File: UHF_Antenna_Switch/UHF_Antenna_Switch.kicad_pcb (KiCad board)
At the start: 2 copper layers, 157.2 x 60 mm, 44 parts, among them J1 Conn_N_Type_Female, J2 Conn_SO-239, J3 Conn_SMA_Female, J4 Screw_Terminal_01x04, J5 Conn_02x03_Odd_Even, K1 HF3-51, K2 HF3-51, Q2 2N7002, Q3 2N7002, SW1 SW_SP3T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

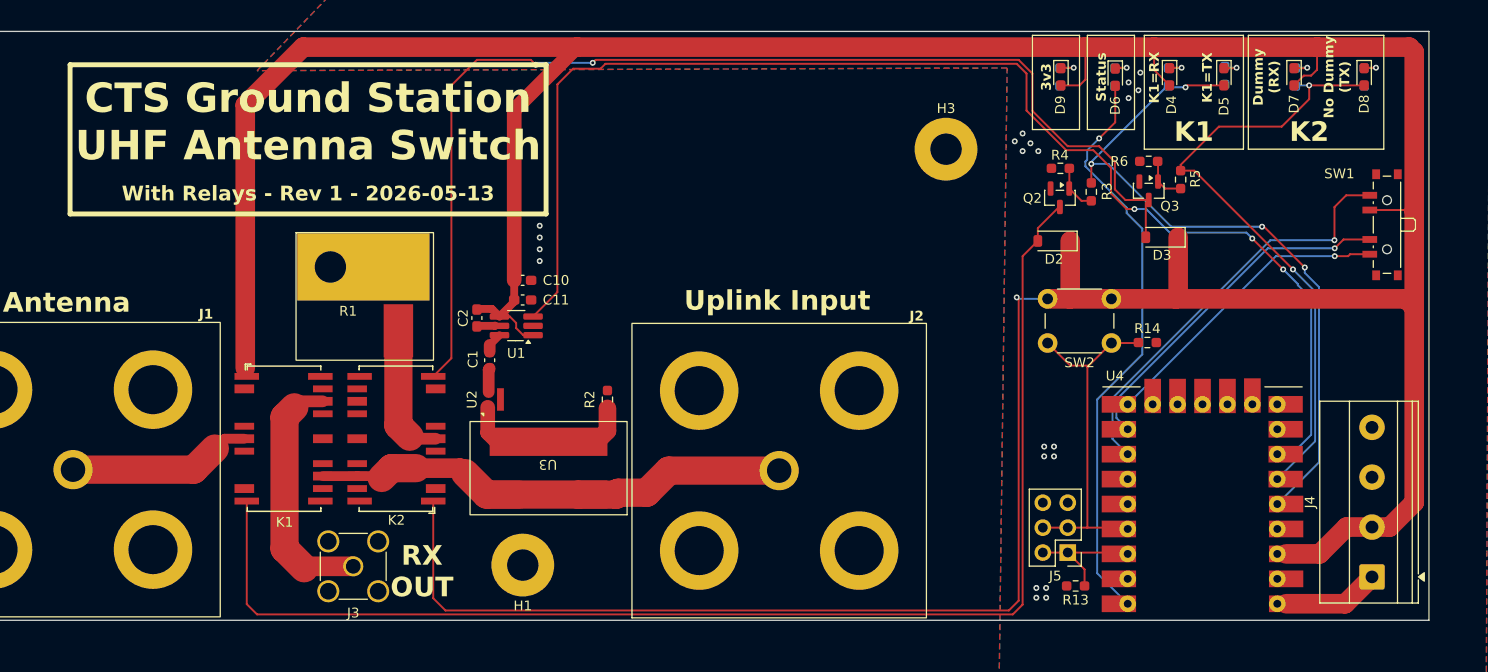
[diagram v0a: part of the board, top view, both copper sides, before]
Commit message: PCB: Resolve DRC issues
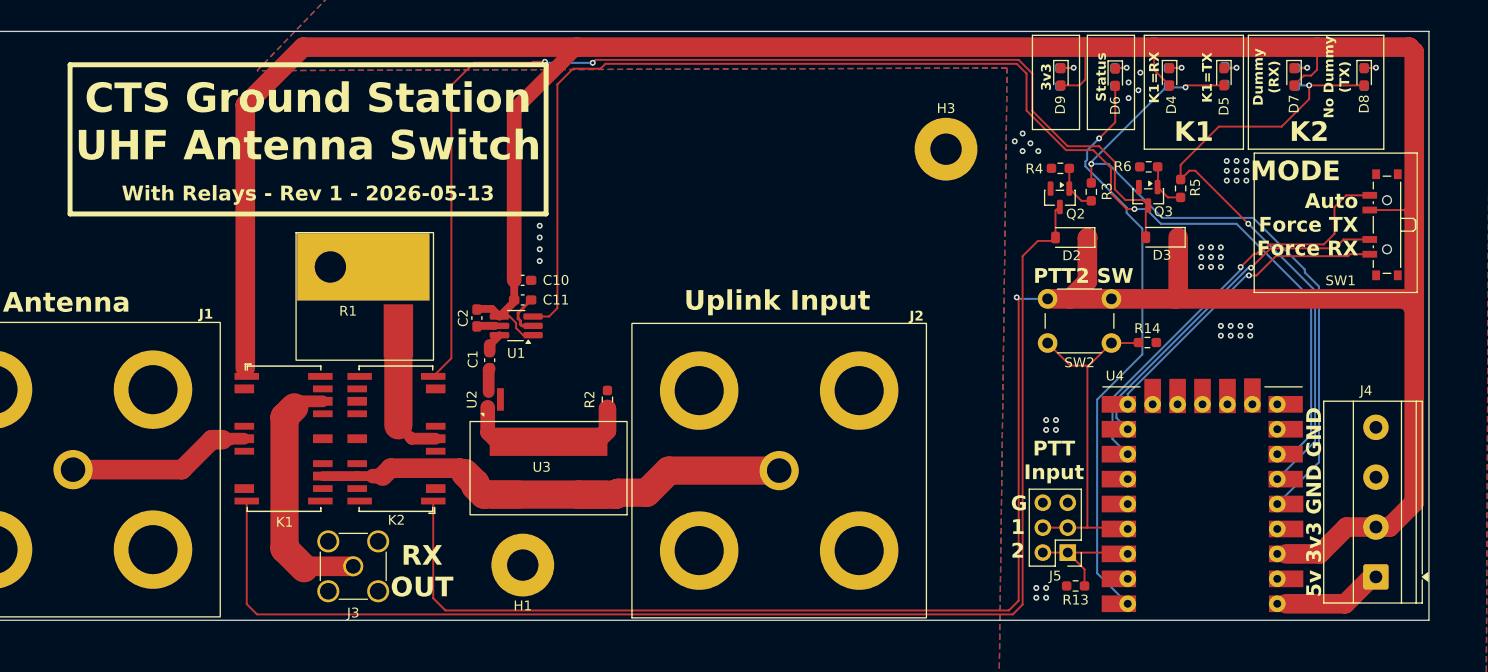
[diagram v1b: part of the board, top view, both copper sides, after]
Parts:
- moved D2 1.83 mm to (195.8, 96.0)
- moved R5 0.90 mm to (206.9, 91.0)
- moved Q3 0.56 mm to (203.6, 91.8)
- moved R6 0.56 mm to (203.7, 88.8)
- moved J4 0.40 mm to (226.8, 130.6)
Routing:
- net GNDS: track 0.00 -> 4.47 mm
- net Net-(U3-ISOLATED): track 5.75 -> 3.86 mm
- net /Relay_K2/RF_COMMON: track 14.0 -> 12.4 mm
- net TX_EN_RELAY_K2: track 64.4 -> 65.6 mm
- net /Relay_K1/RF_NO: track 21.6 -> 22.6 mm
- net TX_DETECTED: track 134.2 -> 135.1 mm, vias 3 -> 1
- net +3V3: track 422.9 -> 423.7 mm
- net Net-(D3-A): track 116.7 -> 115.9 mm
- net /Relay_K1/RF_COMMON: track 18.8 -> 18.1 mm
- net Net-(U4-GP8): track 31.0 -> 31.6 mm
- net TX_EN_RELAY_K1: track 71.6 -> 71.1 mm, vias 4 -> 2
- net GNDD: vias 17 -> 43
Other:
- board text added: "5v 3v3 GND GND"
- board text added: "Auto Force TX Force RX"
- board text added: "G 1 2"
- board text added: "MODE"
- board text added: "PTT Input"
- board text added: "PTT2 SW"

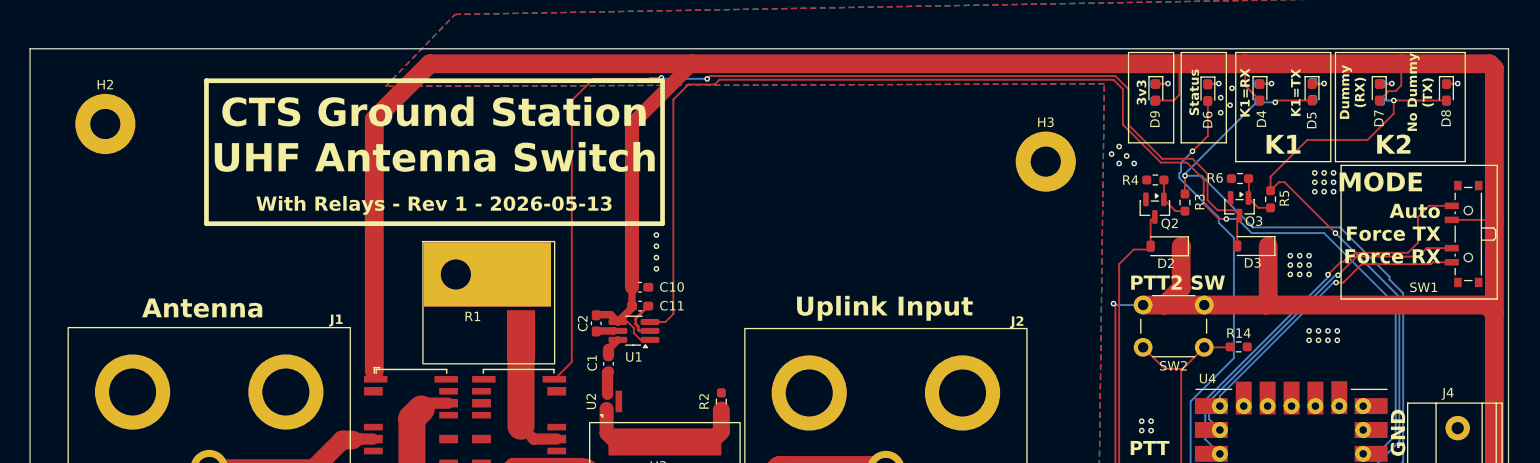
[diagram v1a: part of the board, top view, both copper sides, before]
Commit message: PCB: Add 4th mounting hole
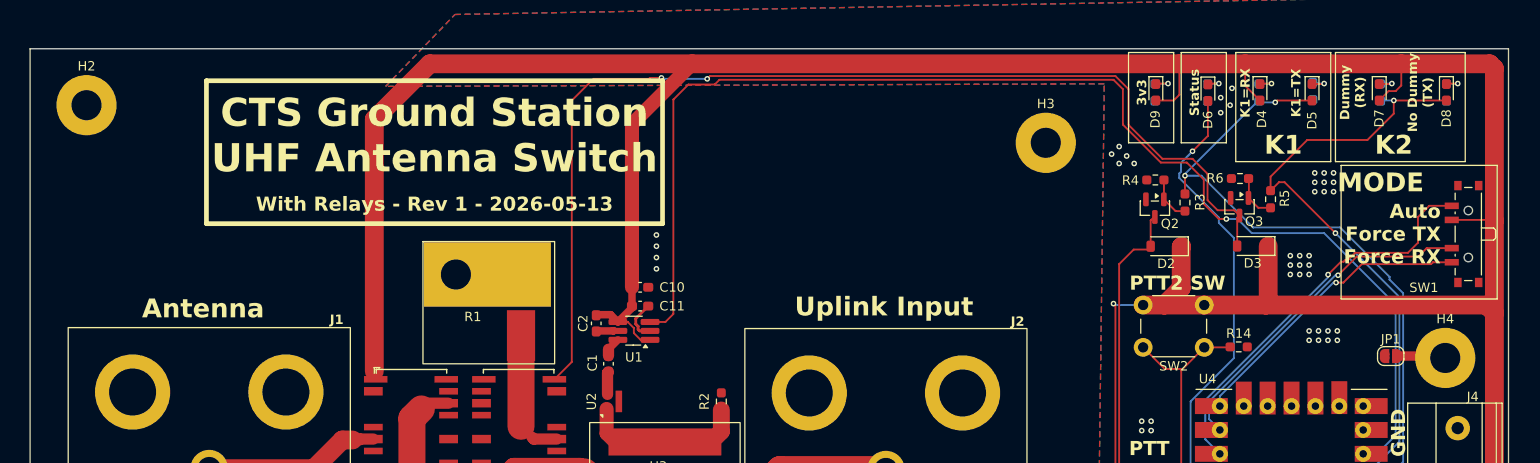
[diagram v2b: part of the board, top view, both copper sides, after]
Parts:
- added H4: MountingHole_Pad, MountingHole:MountingHole_3.2mm_M3_Pad, F.Cu at (225.5, 107.9)
- added JP1: SolderJumper_2_Open, Jumper:SolderJumper-2_P1.3mm_Open_RoundedPad1.0x1.5mm, F.Cu at (219.7, 107.7)
- moved H2 2.83 mm to (81.0, 81.0)
- moved H3 2.00 mm to (183.0, 85.0)
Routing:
- net Net-(JP1-B): track 0.00 -> 5.23 mm

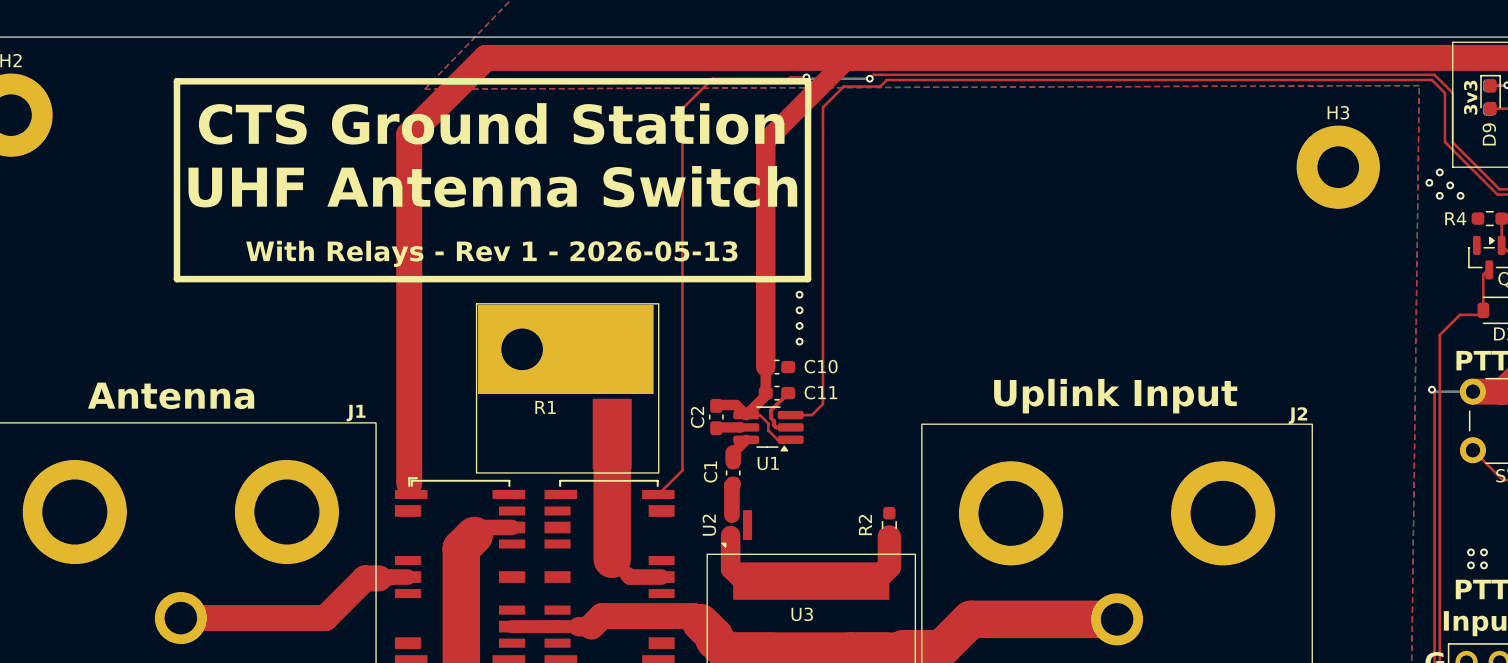
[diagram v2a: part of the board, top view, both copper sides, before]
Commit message: Bond RF and Digital GNDs
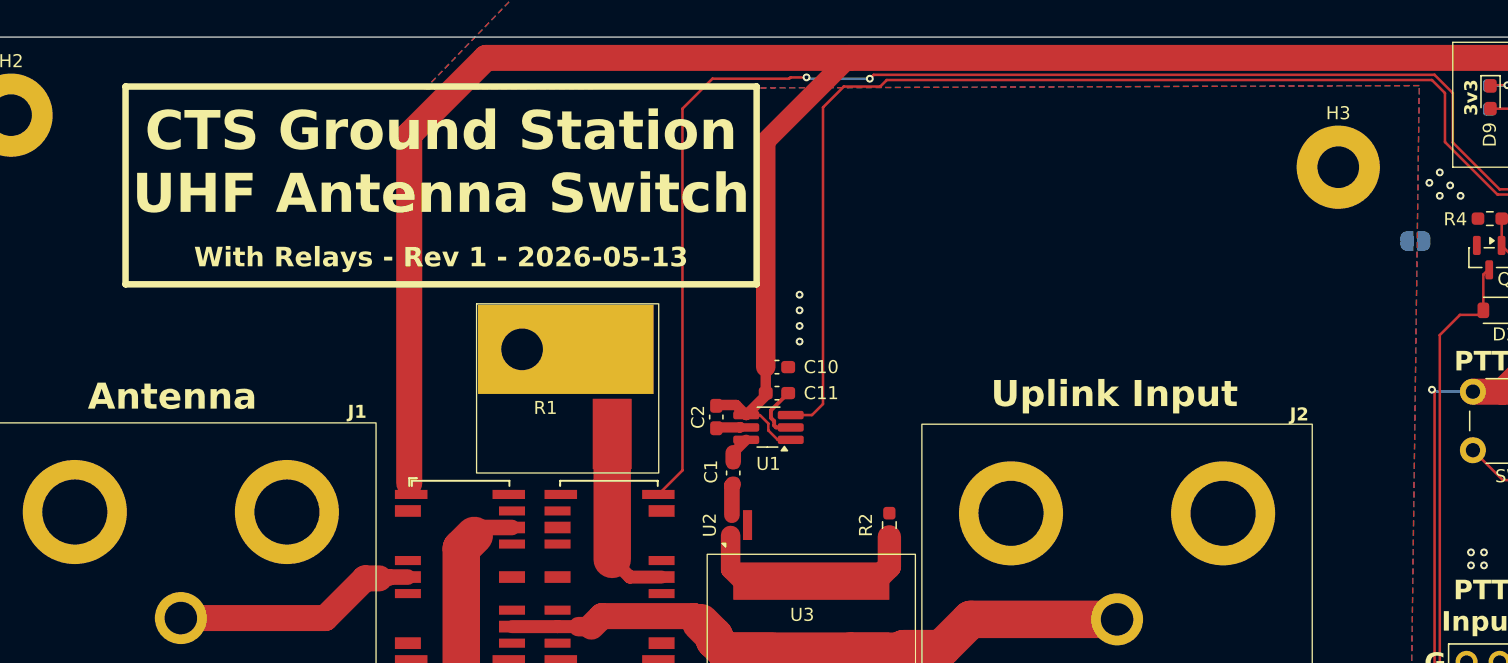
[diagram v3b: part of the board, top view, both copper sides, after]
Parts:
- added JP2: SolderJumper_2_Open, Jumper:SolderJumper-2_P1.3mm_Open_RoundedPad1.0x1.5mm, B.Cu at (188.9, 90.7)
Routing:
- net /Relay_K2/RF_COMMON: track 12.4 -> 14.0 mm
